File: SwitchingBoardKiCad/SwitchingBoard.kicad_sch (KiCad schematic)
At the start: 53 parts, among them J1 Screw_Terminal_01x02, J2 Screw_Terminal_01x02, J3 Screw_Terminal_01x02, J4 Screw_Terminal_01x02, J5 Screw_Terminal_01x02, J6 Screw_Terminal_01x03, J7 Screw_Terminal_01x02, J8 Screw_Terminal_01x02, J9 Screw_Terminal_01x02, K1 FINDER-30.22, Q1 BT169G, Q2 BTB16-800CW, Q3 BTB16-800CW

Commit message: Fixed TRIAC symbol and tweaked layout further.
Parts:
- removed Q1: BT169G, Package_TO_SOT_THT:TO-92_Inline, symbol Triac_Thyristor:BT169G
- added Q1: Q_TRIAC_A2GA1, Package_TO_SOT_THT:TO-92L_Inline, symbol Device:Q_TRIAC_A2GA1
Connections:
- net Control Live: now also Q1.1 (A2)
- net Timed live: now also Q1.3 (A1)
- net at J8.1 (Pin_1): now also Q3.3 (G), R14.2; no longer R13.1
- net at J3.1 (Pin_1), R3.2: now also Q1.2 (G)
- new net: J8.2 (Pin_2), R13.1
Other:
- moved on the sheet: J8
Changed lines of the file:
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@@
     (pin "2")
   )
-  (symbol (lib_id "Connector:Screw_Terminal_01x02") (at 212.09 45.72 0) (mirror y) (unit 1)
+  (symbol (lib_id "Connector:Screw_Terminal_01x02") (at 212.09 48.26 180) (unit 1)
     (in_bom yes) (on_board yes) (fields_autoplaced)
     (property "Reference" "J8" (id 0) (at 212.09 39.37 0))
     (property "Value" "Screw_Terminal_01x02" (id 1) (at 212.09 41.91 0))
-    (property "Footprint" "TerminalBlock:TerminalBlock_Altech_AK300-2_P5.00mm" (id 2) (at 212.09 45.72 0)
-      (effects (font (size 1.27 1.27)) hide)
-    )
-    (property "Datasheet" "~" (id 3) (at 212.09 45.72 0)
+    (property "Footprint" "TerminalBlock:TerminalBlock_Altech_AK300-2_P5.00mm" (id 2) (at 212.09 48.26 0)
+      (effects (font (size 1.27 1.27)) hide)
+    )
+    (property "Datasheet" "~" (id 3) (at 212.09 48.26 0)
       (effects (font (size 1.27 1.27)) hide)
     )
@@
     (pin "1")
     (pin "2")
+  )
+  (symbol (lib_id "Device:Q_TRIAC_A2GA1") (at 113.03 49.53 0) (unit 1)
+    (in_bom yes) (on_board yes) (fields_autoplaced)
+    (property "Reference" "Q1" (id 0) (at 116.84 48.8441 0)
+      (effects (font (size 1.27 1.27)) (justify left))
+    )
+    (property "Value" "Q_TRIAC_A2GA1" (id 1) (at 116.84 51.3841 0)
+      (effects (font (size 1.27 1.27)) (justify left))
+    )
+    (property "Footprint" "Package_TO_SOT_THT:TO-92L_Inline" (id 2) (at 114.935 48.895 90)
+      (effects (font (size 1.27 1.27)) hide)
+    )
+    (property "Datasheet" "~" (id 3) (at 113.03 49.53 90)
+      (effects (font (size 1.27 1.27)) hide)
+    )
+    (pin "1")
+    (pin "2")
+    (pin "3")
   )
   (symbol (lib_id "Device:C") (at 173.99 58.42 180) (unit 1)
@@
     )
     (property "Datasheet" "https://www.st.com/resource/en/datasheet/bta16.pdf" (id 3) (at 189.23 49.53 0)
-      (effects (font (size 1.27 1.27)) (justify left) hide)
-    )
-    (pin "1")
-    (pin "2")
-    (pin "3")
-  )
-  (symbol (lib_id "Triac_Thyristor:BT169G") (at 113.03 49.53 0) (unit 1)
-    (in_bom yes) (on_board yes) (fields_autoplaced)
-    (property "Reference" "Q1" (id 0) (at 115.57 48.2599 0)
-      (effects (font (size 1.27 1.27)) (justify left))
-    )
-    (property "Value" "BT169G" (id 1) (at 115.57 50.7999 0)
-      (effects (font (size 1.27 1.27)) (justify left))
-    )
-    (property "Footprint" "Package_TO_SOT_THT:TO-92_Inline" (id 2) (at 115.57 51.435 0)
-      (effects (font (size 1.27 1.27) italic) (justify left) hide)
-    )
-    (property "Datasheet" "https://media.digikey.com/pdf/Data%20Sheets/NXP%20PDFs/BT169_Series.pdf" (id 3) (at 113.03 49.53 0)
       (effects (font (size 1.27 1.27)) (justify left) hide)
     )
@@
       (reference "K1") (unit 1) (value "FINDER-30.22") (footprint "Relay_THT:Relay_DPDT_Finder_40.52")
     )
-    (path "/b29a4364-a9f7-4104-a9f6-bab781c255e6"
-      (reference "Q1") (unit 1) (value "BT169G") (footprint "Package_TO_SOT_THT:TO-92_Inline")
+    (path "/7943b9ac-8cf2-46aa-8b2f-f9424a96c4cc"
+      (reference "Q1") (unit 1) (value "Q_TRIAC_A2GA1") (footprint "Package_TO_SOT_THT:TO-92L_Inline")
     )
     (path "/ae3f60f6-bcec-4ac2-b315-0c6f8465db71"

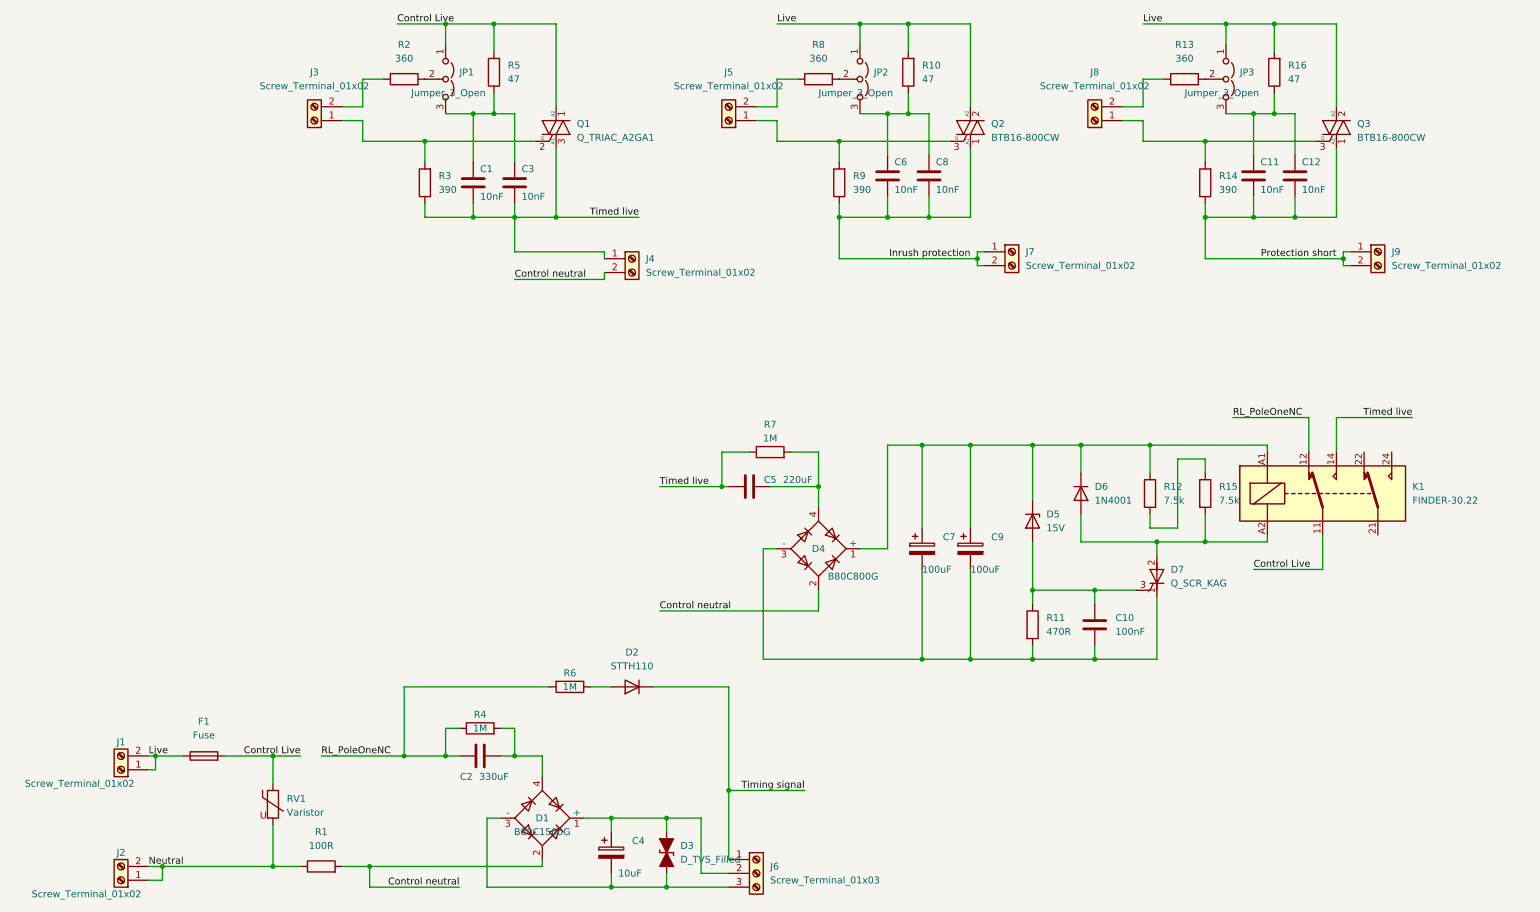
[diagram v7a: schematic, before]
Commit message: Added duplicated resistors to hit worst case voltage ratings.
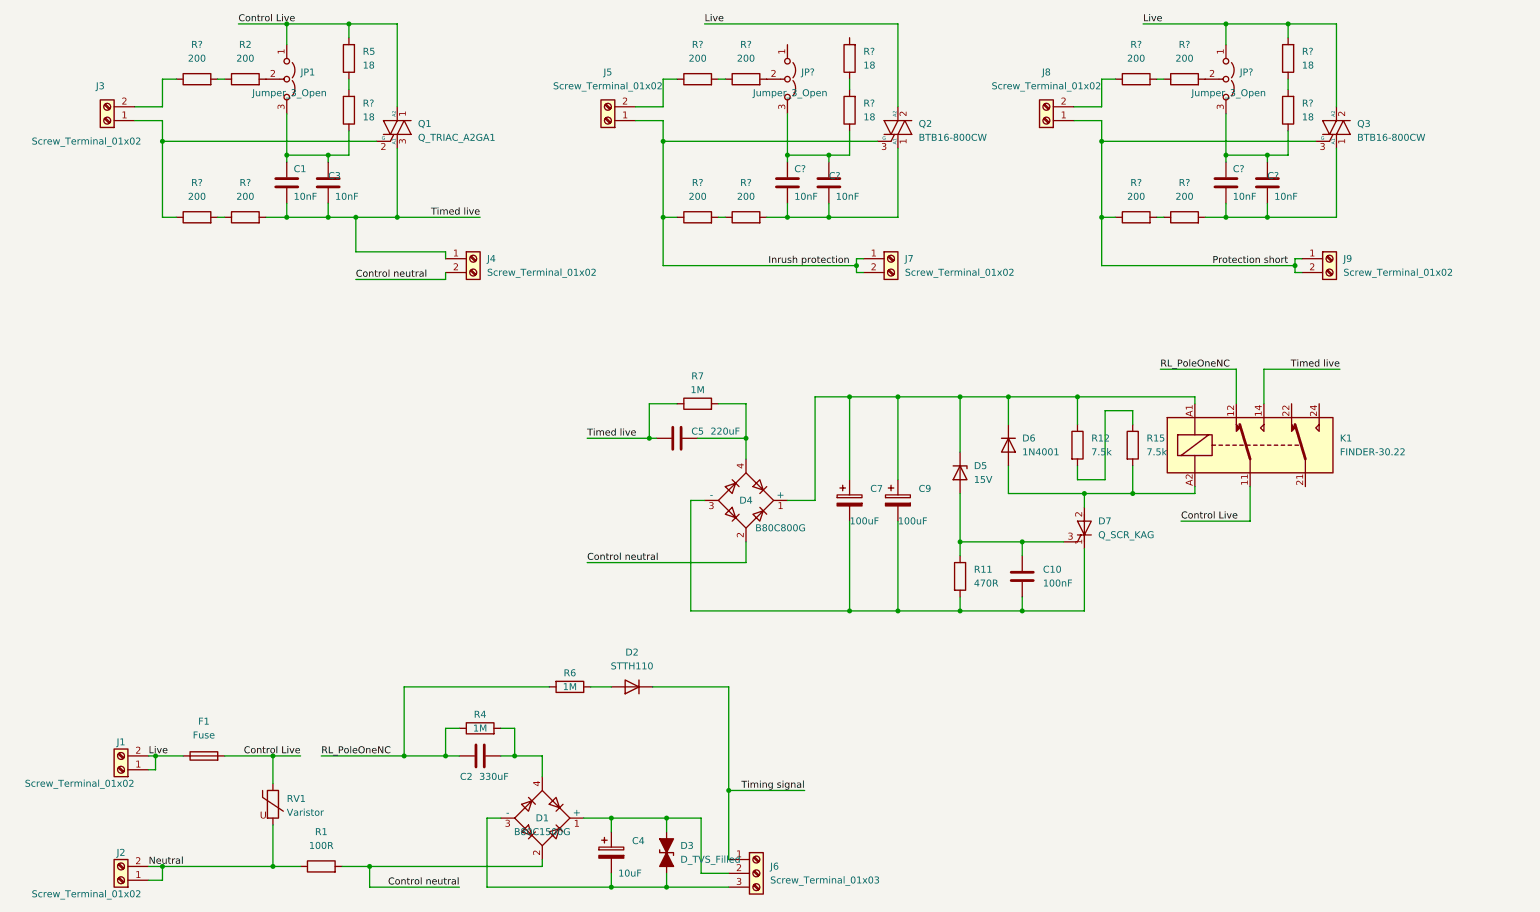
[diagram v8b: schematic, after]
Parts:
- removed C11, C12, C6, C8: 10nF, Capacitor_THT:C_Rect_L18.0mm_W5.0mm_P15.00mm_FKS3_FKP3, symbol Device:C
- removed JP2, JP3: Jumper_3_Open, TerminalBlock_4Ucon:TerminalBlock_4Ucon_1x03_P3.50mm_Horizontal, symbol Jumper:Jumper_3_Open
- removed R10, R16: 47, Resistor_THT:R_Axial_DIN0207_L6.3mm_D2.5mm_P10.16mm_Horizontal, symbol Device:R
- removed R13, R8: 360, Resistor_THT:R_Axial_DIN0207_L6.3mm_D2.5mm_P10.16mm_Horizontal, symbol Device:R
- removed R14, R3, R9: 390, Resistor_THT:R_Axial_DIN0207_L6.3mm_D2.5mm_P10.16mm_Horizontal, symbol Device:R
- added C? (x4): 10nF, Capacitor_THT:C_Rect_L18.0mm_W5.0mm_P15.00mm_FKS3_FKP3, symbol Device:C
- added JP? (x2): Jumper_3_Open, TerminalBlock_4Ucon:TerminalBlock_4Ucon_1x03_P3.50mm_Horizontal, symbol Jumper:Jumper_3_Open
- added R? (x11): 200, Resistor_THT:R_Axial_DIN0207_L6.3mm_D2.5mm_P10.16mm_Horizontal, symbol Device:R
- added R? (x5): 18, Resistor_THT:R_Axial_DIN0207_L6.3mm_D2.5mm_P10.16mm_Horizontal, symbol Device:R
- R2: value 360 -> 200
- R5: value 47 -> 18
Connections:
- net Inrush protection: now also J5.1 (Pin_1), Q2.3 (G), R?.1; no longer Q2.1 (A1)
- net Live: now also JP?.1 (A), R?.2
- net Protection short: now also J8.1 (Pin_1), Q3.3 (G), R?.1; no longer Q3.1 (A1)
- net Timed live: now also R?.2
- net at C1.2, C3.2, JP1.3 (B): now also R?.1; no longer R5.1
- net at J8.2 (Pin_2): now also R?.1
- net at J3.1 (Pin_1), Q1.2 (G): now also R?.1
- net at J5.2 (Pin_2): now also R?.1
- net at J3.2 (Pin_2): now also R?.1; no longer R2.1
- new net: R?.1, R?.2 (x7)
- new net: JP?.2 (C), R?.2 (x2)
- new net: C?.2, C?.2, JP?.3 (B), R?.1 (x2)
- new net: C?.1, C?.1, Q3.1 (A1), R?.2
- new net: C?.1, C?.1, Q2.1 (A1), R?.2
- new net: R2.1, R?.2
- new net: R5.1, R?.2
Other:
- moved on the sheet: C1, C10, C3, C5, C7, C9, D4, D5, D6, D7, J3, J4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
